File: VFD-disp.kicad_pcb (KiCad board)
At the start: 2 copper layers, 120.2 x 65.5 mm, 97 parts, among them J1 USB_C_Receptacle_USB2.0_14P, J2 Conn_02x04_Odd_Even, J3 Jack-DC, J4 Conn_02x04_Odd_Even, J5 Conn_02x04_Odd_Even, J6 Conn_02x04_Odd_Even, Q1 NMOS, Q3 NMOS, SW1 SW_SPST, U1 ESP32-C6-WROOM-1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

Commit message: We need to golf!
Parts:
- J2, J5: value Conn_02x04_Odd_Even -> Conn_02x03_Odd_Even; footprint Connector_PinSocket_2.54mm:PinSocket_2x04_P2.54mm_Horizontal -> Connector_PinSocket_2.54mm:PinSocket_2x03_P2.54mm_Horizontal
- J4, J6: value Conn_02x04_Odd_Even -> Conn_02x03_Odd_Even; footprint Connector_PinHeader_2.54mm:PinHeader_2x04_P2.54mm_Horizontal -> Connector_PinHeader_2.54mm:PinHeader_2x03_P2.54mm_Horizontal
- moved J1 30.6 mm to (134.8, 234.2)
- moved J3 25.4 mm to (158.6, 227.4), turned to 0 degrees
- moved F3 21.2 mm to (152.5, 234.2)
- moved J6 11.8 mm to (42.0, 196.9)
- moved J5 11.0 mm to (41.2, 241.5)
- moved J2 7.34 mm to (131.8, 241.5)
- moved J4 6.51 mm to (132.6, 195.9)
- moved C7 1.00 mm to (126.8, 229.5)
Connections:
- J2 pad 2: VBUS -> GND
- J2 pad 4: VBUS -> GND
- J2 pad 5: GND -> VBUS
- J4 pad 2: VBUS -> GND
- J4 pad 4: VBUS -> GND
- J4 pad 5: GND -> VBUS
- J5 pad 6: GND -> RX2
- J6 pad 6: GND -> TX1
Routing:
- net RX2: track 124.7 -> 0.00 mm, vias 2 -> 0
- net +3.3V: track 171.6 -> 65.8 mm, vias 10 -> 4
- net VBUS: track 243.7 -> 172.9 mm, vias 14 -> 11
- net +5V: track 127.9 -> 105.5 mm, vias 6 -> 5
- net GND: track 124.8 -> 107.7 mm, vias 59 -> 58
- net FORWARD_DETECT: track 74.4 -> 61.4 mm
- net RX1: track 87.1 -> 74.4 mm
- net Net-(Q3-G): track 17.0 -> 4.62 mm
- net TX2: track 126.4 -> 114.9 mm, vias 2 -> 1
- net Net-(Q1-G): track 18.7 -> 8.08 mm
- net TX1: track 85.5 -> 74.9 mm
- net BACKWARD_DETECT: track 111.9 -> 101.7 mm, vias 3 -> 2
- net Net-(D2-K): track 19.6 -> 15.4 mm
- net Net-(U1-GPIO1/ADC1_CH1/XTAL_32K_N): track 12.8 -> 10.1 mm
- net VPP: track 81.6 -> 79.7 mm
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- added copper zone on In2.Cu, net +3.3V
- added copper zone on In1.Cu, net GND
- removed copper zone on B.Cu, net GND
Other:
- board size 120.2 x 65.5 mm -> 99.6 x 65.5 mm
- copper layers 2 -> 4

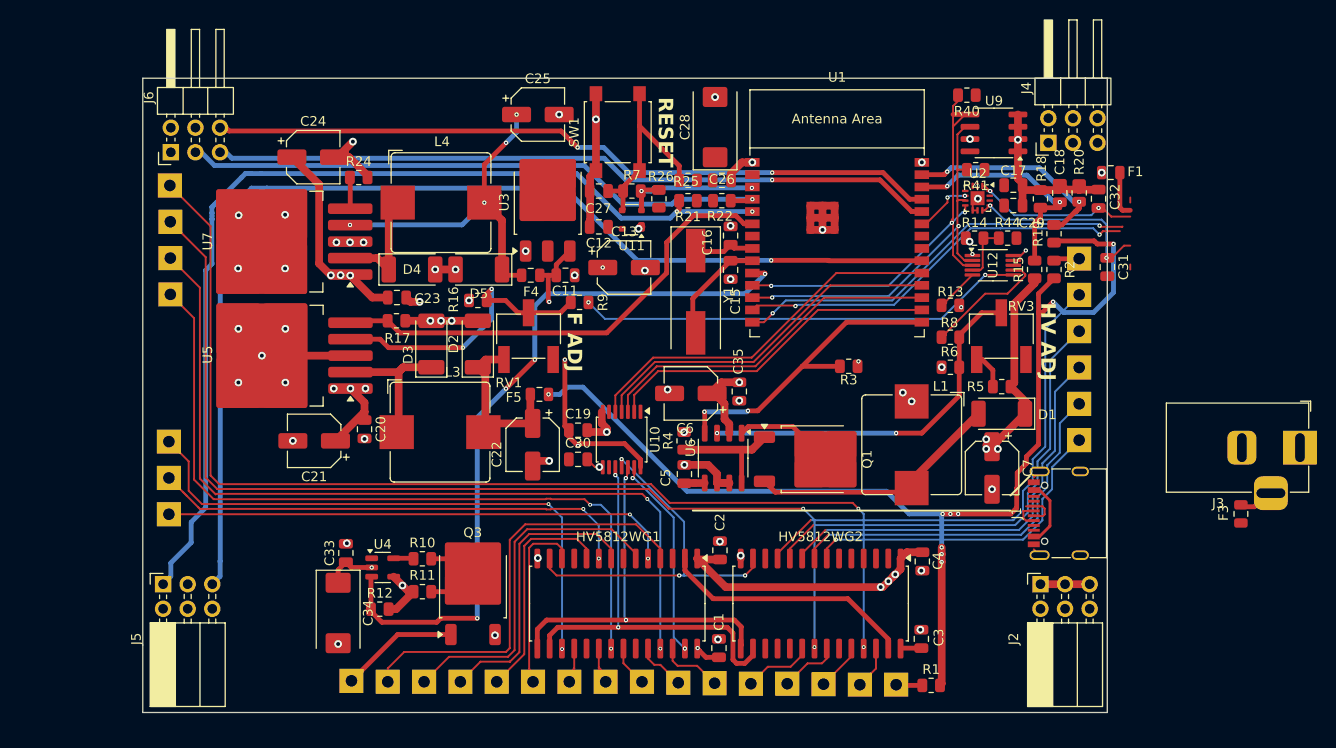
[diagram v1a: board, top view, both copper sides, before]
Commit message: Reroute pcb
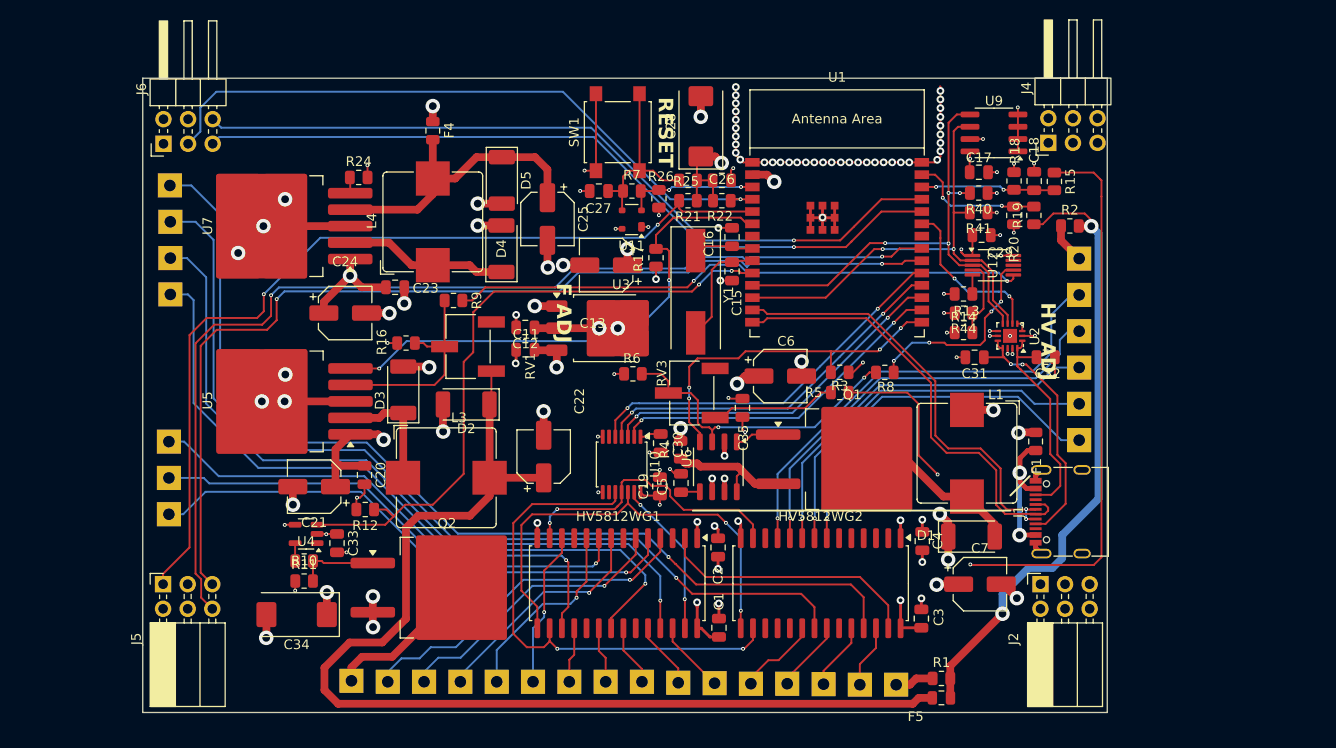
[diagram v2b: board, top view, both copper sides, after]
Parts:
- removed F3: Fuse, Fuse:Fuse_0805_2012Metric
- removed J3: Jack-DC, Connector_BarrelJack:BarrelJack_Horizontal
- removed Q3: NMOS, Package_TO_SOT_SMD:TO-252-2
- added Q2: Q_NMOS_GDS, Package_TO_SOT_SMD:TO-263-2, F.Cu at (70.5, 241.9)
- Q1: value NMOS -> Q_NMOS_GDS; footprint Package_TO_SOT_SMD:TO-252-2 -> Package_TO_SOT_SMD:TO-263-2
- moved F5 52.0 mm to (121.6, 253.2)
- moved R6 32.8 mm to (89.7, 219.8)
- moved RV3 32.5 mm to (95.8, 221.8), turned to -90 degrees
- moved F1 28.8 mm to (131.3, 226.8), turned to 90 degrees
- moved R17 27.6 mm to (92.1, 207.8), turned to -90 degrees
- moved F4 18.0 mm to (69.0, 194.7), turned to 90 degrees
- moved C32 17.2 mm to (132.3, 218.1), turned to 0 degrees
- moved R5 16.7 mm to (111.1, 221.7)
- moved C31 16.6 mm to (125.0, 218.1), turned to 180 degrees
- moved C24 16.4 mm to (60.0, 213.5)
- moved U2 14.6 mm to (128.7, 215.9), turned to 180 degrees
- moved U3 14.3 mm to (86.9, 215.1), turned to 0 degrees
- moved D1 13.1 mm to (124.7, 236.6), turned to 0 degrees
- moved R9 13.0 mm to (71.2, 212.2)
- moved C12 12.9 mm to (78.6, 215.0)
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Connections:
- Q1 pad 1: Net-(Q1-D) -> Net-(Q1-G)
- Q1 pad 2: Net-(Q1-G) -> Net-(D1-A)
- Q1 pad 3: Net-(D1-A) -> Net-(Q1-S)
- R4 pad 1: Net-(Q1-D) -> Net-(Q1-S)
- U6 pad 8: Net-(Q1-D) -> Net-(Q1-S)
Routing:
- net VBUS: track 172.9 -> 35.2 mm, vias 11 -> 8
- net RX2: track 0.00 -> 108.7 mm, vias 0 -> 2
- net Net-(D2-K): track 15.4 -> 114.4 mm
- net +5V: track 105.5 -> 23.5 mm, vias 5 -> 7
- net GND: track 107.7 -> 168.5 mm, vias 58 -> 106
- net F: track 121.2 -> 65.4 mm, vias 9 -> 2
- net +3.3V: track 65.8 -> 41.9 mm, vias 4 -> 18
- net Net-(Q1-S): track 0.00 -> 13.5 mm
- net F_ADJ: track 46.5 -> 59.6 mm
- net Net-(Q1-D): track 12.3 -> 0.00 mm
- net PD_INT: track 5.51 -> 17.1 mm
- net GREEN1: track 114.5 -> 103.3 mm, vias 2 -> 1
- net GREEN2: track 105.7 -> 94.8 mm, vias 2 -> 1
- net Net-(U1-GPIO3/ADC1_CH3): track 24.0 -> 13.9 mm
- net GREEN3: track 87.2 -> 77.2 mm, vias 2 -> 1
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- added copper zone on In2.Cu, net +5V
- added copper zone on In2.Cu, net VBUS
- added copper zone on In2.Cu, net VPP

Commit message: Add chonky cermaics caps to be safe...
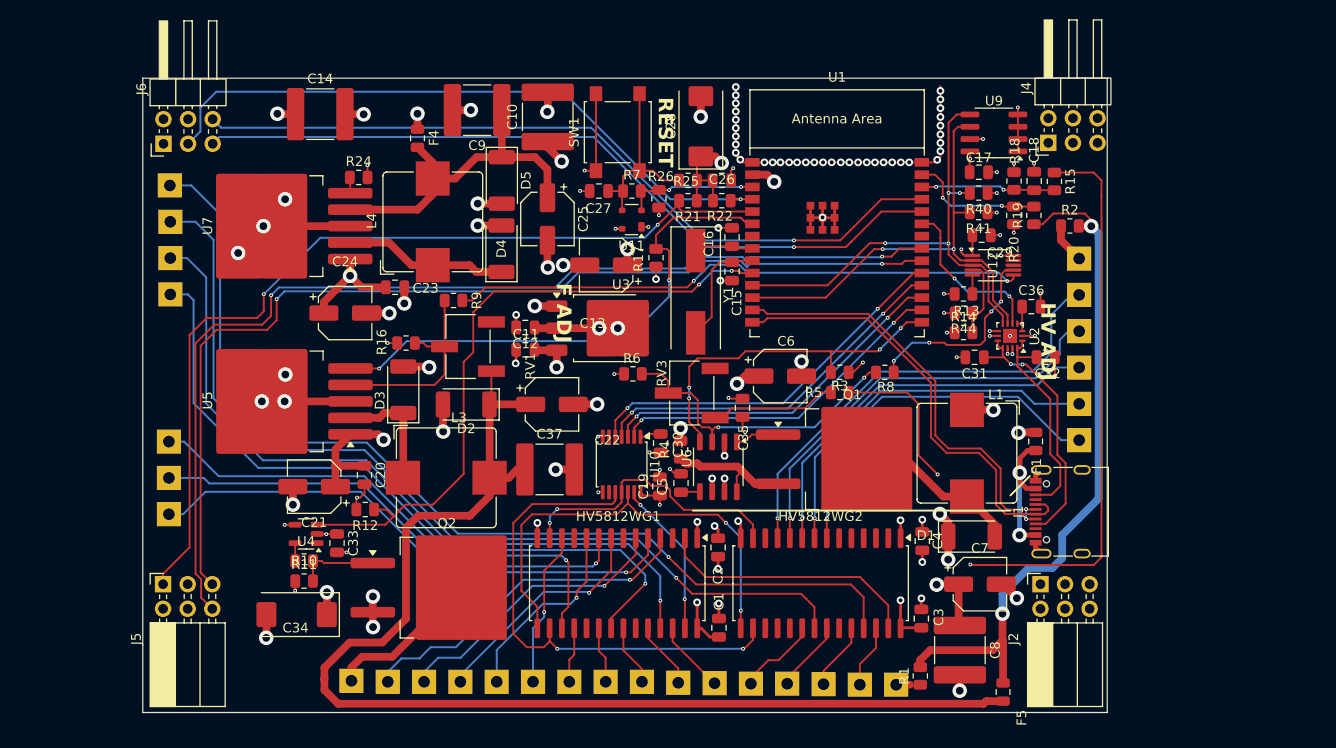
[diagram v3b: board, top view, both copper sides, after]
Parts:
- added C10: C, Capacitor_SMD:C_2220_5750Metric, F.Cu at (80.9, 193.2)
- added C14: C, Capacitor_SMD:C_2220_5750Metric, F.Cu at (57.4, 193.0)
- added C36: C, Capacitor_SMD:C_0805_2012Metric, F.Cu at (130.9, 212.8)
- added C37: C, Capacitor_SMD:C_2220_5750Metric, F.Cu at (81.1, 229.7)
- added C8: C, Capacitor_SMD:C_2220_5750Metric, F.Cu at (123.5, 248.3)
- added C9: C, Capacitor_SMD:C_2220_5750Metric, F.Cu at (73.6, 192.6)
- moved F5 6.40 mm to (127.9, 252.6), turned to 90 degrees
- moved C22 5.46 mm to (81.4, 222.9), turned to 0 degrees
- moved R1 2.20 mm to (119.4, 251.0), turned to 90 degrees
- moved F4 1.76 mm to (67.5, 195.5)
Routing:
- net GND: track 168.5 -> 179.3 mm, vias 106 -> 112
- net Net-(D2-K): track 114.4 -> 124.3 mm
- net F: track 65.4 -> 71.7 mm
- net Net-(D5-K): track 31.0 -> 35.7 mm
- net +3.3V: track 41.9 -> 46.3 mm, vias 18 -> 19
- net VPP: track 87.4 -> 91.7 mm
- net Net-(IVLM3-5/1-F-Pad7): track 4.03 -> 1.42 mm
- net VBUS: track 35.2 -> 37.1 mm, vias 8 -> 9

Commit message: Finish pcb
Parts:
- removed D5: D_Zener, Diode_SMD:D_MELF
- added C38: 10uF, Capacitor_SMD:C_1206_3216Metric, F.Cu at (61.8, 197.5)
- added C39: 10uF, Capacitor_SMD:C_1206_3216Metric, F.Cu at (61.8, 192.9)
- added C40: C, Capacitor_SMD:C_0805_2012Metric, F.Cu at (61.3, 195.3)
- added C41: C, Capacitor_SMD:C_0805_2012Metric, F.Cu at (57.0, 190.6)
- added D6: BZV55B7V5, Diode_SMD:D_MiniMELF, F.Cu at (49.0, 211.6)
- added Q3: Q_NPN_BEC, Package_TO_SOT_SMD:SOT-23, F.Cu at (53.8, 212.1)
- added R23: R, Resistor_SMD:R_0805_2012Metric, F.Cu at (65.3, 196.9)
- added R27: R, Resistor_SMD:R_0805_2012Metric, F.Cu at (65.3, 193.5)
- added R28: R, Resistor_SMD:R_0805_2012Metric, F.Cu at (77.4, 199.4)
- added R29: R, Resistor_SMD:R_0805_2012Metric, F.Cu at (49.8, 214.8)
- added R30: R, Resistor_SMD:R_0805_2012Metric, F.Cu at (53.8, 215.0)
- added U13: TPS2116DRL, Package_TO_SOT_SMD:SOT-583-8, F.Cu at (68.3, 196.0)
- added U14: KF50BDT, Package_TO_SOT_SMD:TO-252-2, F.Cu at (52.9, 195.2)
- added U8: USBLC6-2P6, Package_TO_SOT_SMD:SOT-666, F.Cu at (120.3, 220.3)
- D1, D2, D3, D4: footprint Diode_SMD:D_MELF -> Diode_SMD:D_SMB
- moved C14 42.0 mm to (48.0, 233.9), turned to 90 degrees
- moved R24 19.8 mm to (45.1, 210.6), turned to -90 degrees
- moved F4 2.49 mm to (68.3, 193.1)
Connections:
- C25 pad 1: Net-(D5-K) -> Net-(U13-MODE)
- C9 pad 1: Net-(D5-K) -> Net-(U13-MODE)
- F4 pad 1: Net-(D5-K) -> Net-(F4-Pad1)
- L4 pad 2: Net-(D5-K) -> Net-(U13-MODE)
- R24 pad 1: Net-(U7-~{ON}/OFF) -> VBUS
- R24 pad 2: GND -> Net-(D6-K)
- U1 pad 13: USB_D- -> PRE_USB_D-
- U1 pad 14: USB_D+ -> PRE_USB_D+
- U1 pad 7: unconnected-(U1-MTDO/GPIO7-Pad7) -> VBUS_ABOVE_TRESHOLD
- U7 pad 4: Net-(D5-K) -> Net-(U13-MODE)
- U7 pad 5: Net-(U7-~{ON}/OFF) -> Net-(Q3-C)
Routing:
- net Net-(U13-MODE): track 0.00 -> 45.6 mm
- net VBUS_ABOVE_TRESHOLD: track 0.00 -> 43.6 mm, vias 0 -> 4
- net Net-(D5-K): track 35.7 -> 0.00 mm
- net USB_D-: track 45.2 -> 22.5 mm
- net USB_D+: track 46.4 -> 24.4 mm
- net PRE_USB_D-: track 0.00 -> 21.7 mm
- net Net-(U13-VIN2): track 0.00 -> 21.1 mm, vias 0 -> 2
- net PRE_USB_D+: track 0.00 -> 21.0 mm
- net Net-(Q3-C): track 0.00 -> 18.2 mm
- net VBUS: track 37.1 -> 49.7 mm, vias 9 -> 12
- net Net-(F4-Pad1): track 0.00 -> 6.32 mm
- net +3.3V: track 46.3 -> 52.2 mm
- net GND: track 179.3 -> 184.4 mm, vias 112 -> 123
- net Net-(D6-A): track 0.00 -> 4.97 mm
- net Net-(U13-PR1): track 0.00 -> 4.22 mm
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
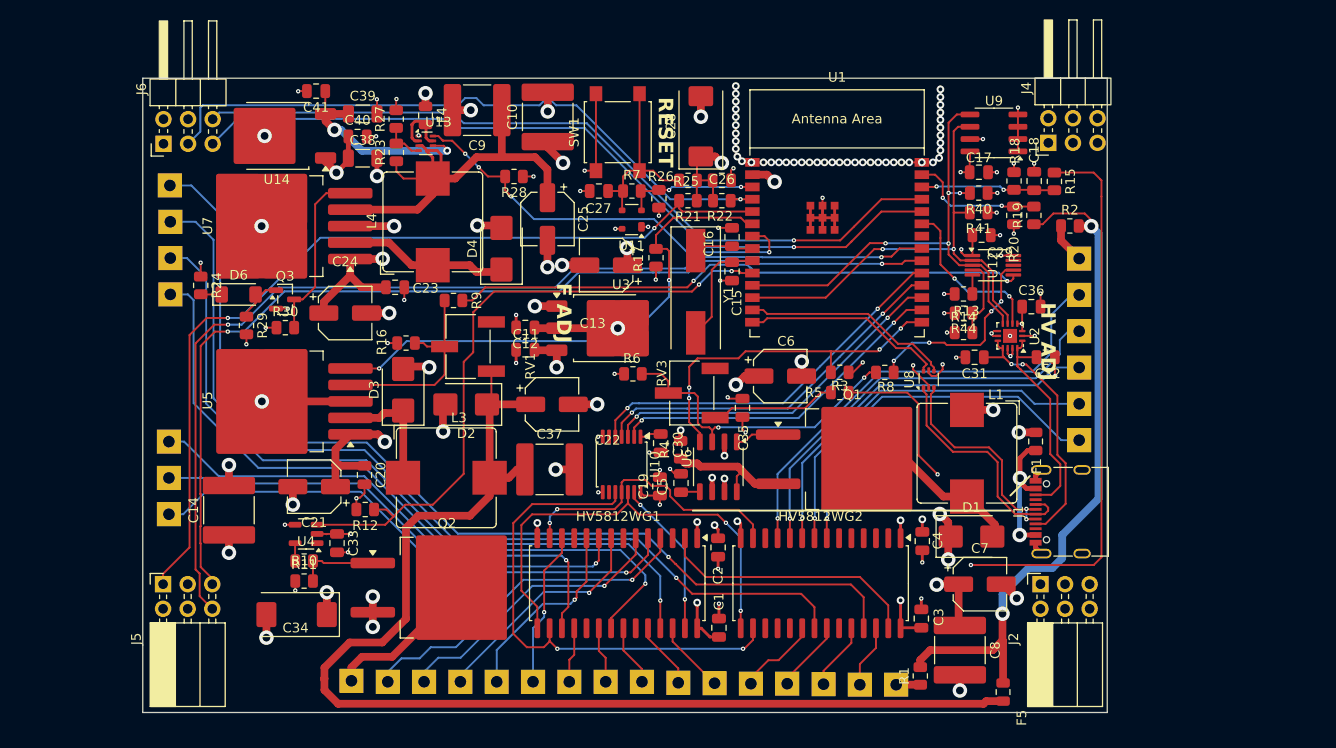
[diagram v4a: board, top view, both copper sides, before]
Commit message: Add mounting holes and some rework
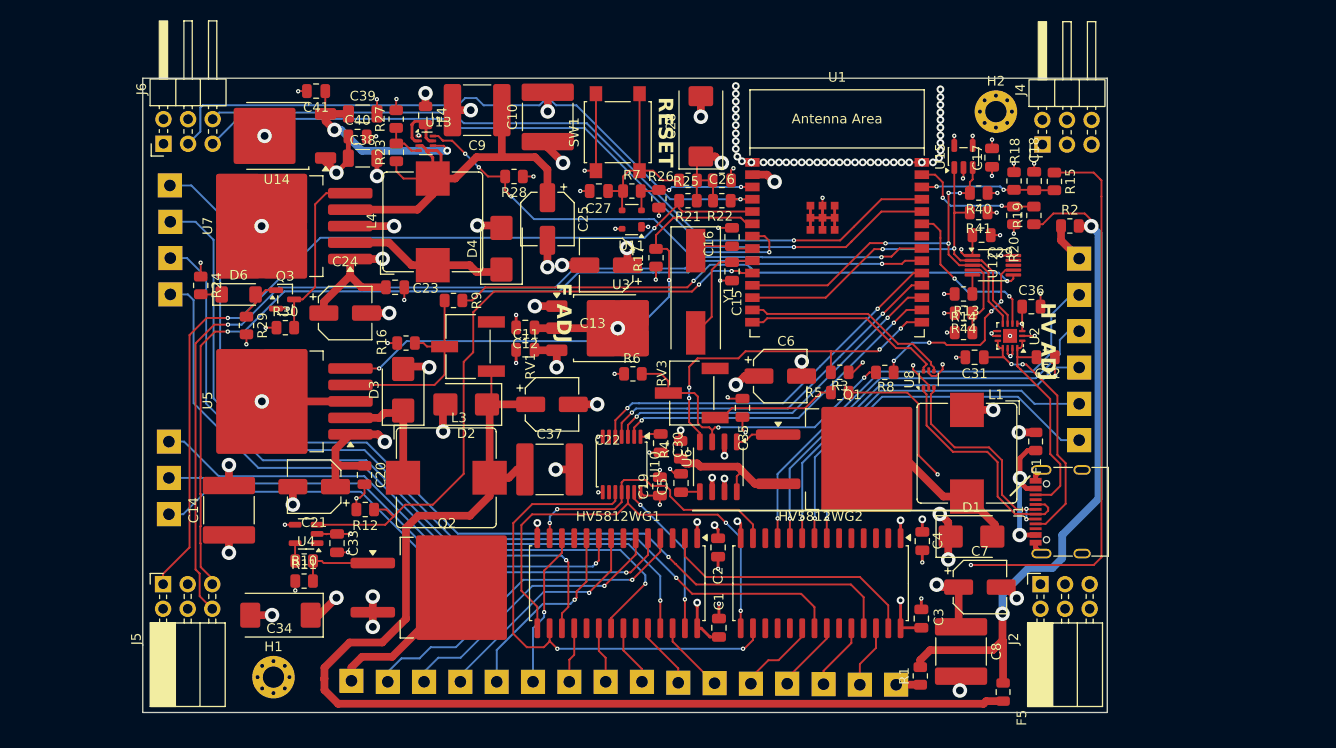
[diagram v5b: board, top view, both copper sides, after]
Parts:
- removed U9: FM24C64B, Package_SO:SOIC-8_3.9x4.9mm_P1.27mm
- added H1: MountingHole_Pad_MP, MountingHole:MountingHole_2.2mm_M2_Pad_Via, F.Cu at (52.6, 251.1)
- added H2: MountingHole_Pad_MP, MountingHole:MountingHole_2.2mm_M2_Pad_Via, F.Cu at (127.2, 192.7)
- added U15: AT24CS01-STUM, Package_TO_SOT_SMD:SOT-23-5, F.Cu at (123.8, 197.3)
- moved C17 2.03 mm to (126.8, 197.4), turned to 90 degrees
- moved C34 1.67 mm to (53.3, 244.7)
- moved J4 0.64 mm to (132.0, 196.1)
- moved C7 0.30 mm to (125.5, 241.8)
- moved C8 0.18 mm to (123.6, 248.4)
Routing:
- net SDA: track 51.2 -> 44.3 mm
- net SCL: track 49.9 -> 44.3 mm
- net GND: track 184.4 -> 180.7 mm
- net +3.3V: track 52.2 -> 51.1 mm, vias 19 -> 20
- net +5V: track 24.8 -> 25.9 mm

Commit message: Fix DRC errors
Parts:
- moved C8 0.70 mm to (123.5, 249.2)
- moved L4 0.45 mm to (68.6, 204.1)
- moved C25 0.41 mm to (81.3, 203.8)
- moved C23 0.31 mm to (64.8, 210.8)
- moved D1 0.22 mm to (124.7, 236.8)
- moved C13 0.20 mm to (87.2, 208.6)
- moved C7 0.20 mm to (125.5, 242.0)
- moved F4 0.20 mm to (68.3, 192.9)
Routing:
- net GND: track 180.7 -> 183.5 mm, vias 123 -> 119
- net Net-(U13-MODE): track 45.6 -> 46.7 mm
- net F: track 71.7 -> 72.6 mm

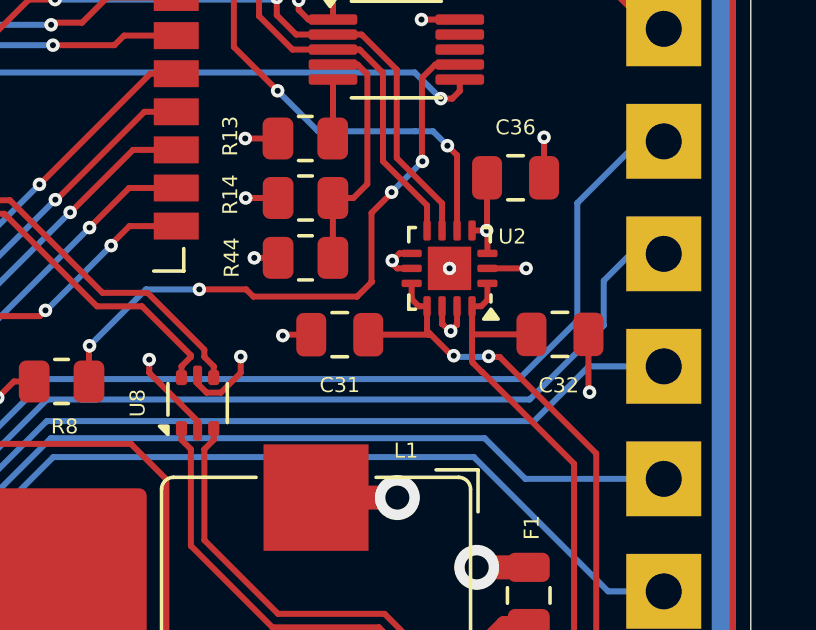
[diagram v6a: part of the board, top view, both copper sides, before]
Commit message: Add CC lines pull down
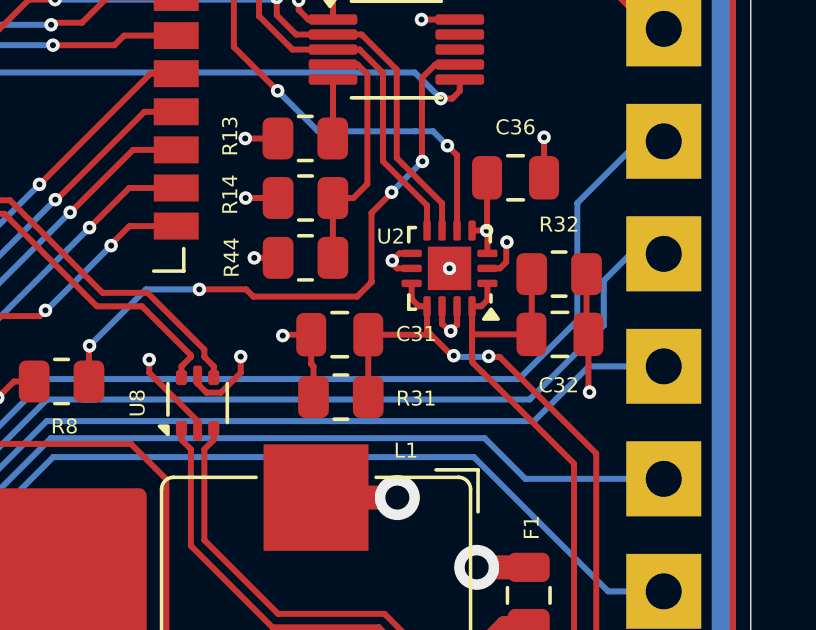
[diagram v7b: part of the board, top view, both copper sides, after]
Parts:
- added R31: 5.1K, Resistor_SMD:R_0805_2012Metric, F.Cu at (125.0, 220.2)
- added R32: 5.1K, Resistor_SMD:R_0805_2012Metric, F.Cu at (132.3, 216.1)
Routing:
- net GND: track 183.5 -> 187.6 mm
- net Net-(J1-CC1): track 26.9 -> 28.9 mm
- net Net-(J1-CC2): track 22.1 -> 24.2 mm

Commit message: Fix screw connections
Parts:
- H1, H2: value MountingHole_Pad_MP -> MountingHole_Pad
- moved H1 94.7 mm to (127.2, 192.7)
- moved H2 94.7 mm to (52.6, 251.1)
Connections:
- H1 pad 1: (no net) -> GND
- H2 pad 1: (no net) -> GND
